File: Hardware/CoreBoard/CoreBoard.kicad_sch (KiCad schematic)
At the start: 86 parts, among them J1 RJ45_LED_Shielded, SW1 SW_Push, SW10 SW_Push, SW11 SW_Push, SW12 SW_Push, SW13 SW_Push, SW14 SW_Push, SW15 SW_Push, SW16 SW_SPDT, SW2 SW_Push, SW3 SW_Push, SW4 SW_Push, SW5 SW_Push, SW6 SW_Push, SW7 SW_Push, SW8 SW_Push, SW9 SW_Push, U1 Teensy4.1_DEV-16771, U3 SHHD003A0A, U4 74HC148, U5 74HC148, U6 74HC00, U7 OKI

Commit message: made rev2 changes and cleaned up traces
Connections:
- net +3V3: no longer U4.5 (EI)
- net BL_RX: now also Conn2.2, U1.34 (RX8); no longer Conn2.8, U1.35 (TX8)
- net BL_TX: now also Conn2.1, U1.35 (TX8); no longer Conn2.9, U1.30 (CRX3)
- net BR_RX: now also U1.15 (A1); no longer U1.17 (A3)
- net BR_TX: now also U1.14 (A0); no longer U1.16 (A2)
- net FL_RX: now also Conn2.8, U1.28 (RX7); no longer Conn2.2, U1.14 (A0)
- net FL_TX: now also Conn2.7, U1.29 (TX7); no longer Conn2.3, U1.38 (A14)
- net FR_RX: now also U1.21 (A7); no longer U1.23 (A9)
- net FR_TX: now also U1.20 (A6); no longer U1.22 (A8)
- net GND: now also Conn2.3, Conn2.6, Conn2.9, U4.5 (EI); no longer Conn2.1, Conn2.4, Conn2.7
- net ML_RX: now also U1.25 (A11); no longer U1.37 (CS3)
- net ML_TX: now also Conn2.4, U1.24 (A10); no longer Conn2.6, U1.36 (CS2)
- net MR_RX: now also U1.16 (A2); no longer U1.21 (A7)
- net MR_TX: now also U1.17 (A3); no longer U1.20 (A6)
- net Out2: now also U1.41 (A17); no longer U1.34 (RX8)
- net ServoPWM1: now also U1.0 (RX1); no longer U1.2 (OUT2)
- net ServoPWM2: now also U1.1 (TX1); no longer U1.3 (LRCLK2)
- net ServoPWM3: now also U1.2 (OUT2); no longer U1.4 (BCLK2)
- net ServoPWM4: now also U1.3 (LRCLK2); no longer U1.5 (IN2)
- net ServoPWM5: now also U1.4 (BCLK2); no longer U1.6 (OUT1D)
- net ServoPWM6: now also U1.5 (IN2); no longer U1.7 (RX2)
- net ServoPWM7: now also U1.6 (OUT1D); no longer U1.8 (TX2)
- net ServoPWM8: now also U1.7 (RX2); no longer U1.9 (OUT1C)
- net ServoPWM9: now also U1.8 (TX2); no longer U1.10 (CS1)
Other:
- note added: "exact changes from rev1: moved FR_TX to 20 moved FR_RX to 21 moved MR_TX to 17 moved MR_RX to 16 moved BR_TX to 14 moved BR_RX to 15 moved FL_TX to 29 moved FL_RX to 28 moved ML_TX to 24 moved ML_RX to 25 moved BL_TX to 35 moved BL_RX to 34 moved Out2 from 34 to 41 moved ServoPWM1 to 0 moved ServoPWM2 to 1 moved ServoPWM3 to 2 moved ServoPWM4 to 3 moved ServoPWM5 to 4 moved ServoPWM6 to 5 moved S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"
- moved on the sheet: U4, U5

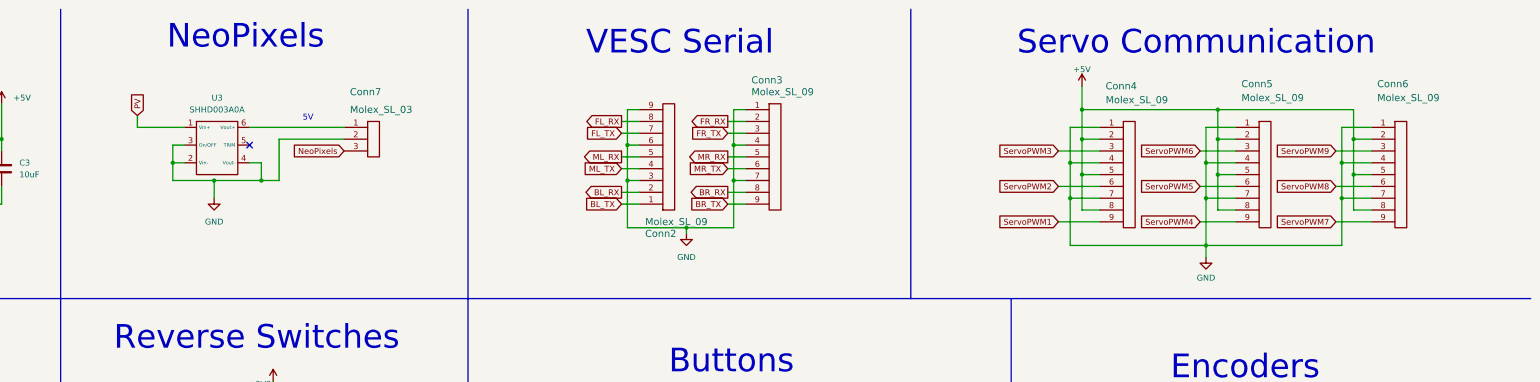
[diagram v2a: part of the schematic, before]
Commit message: added accelerometer and touch-ups
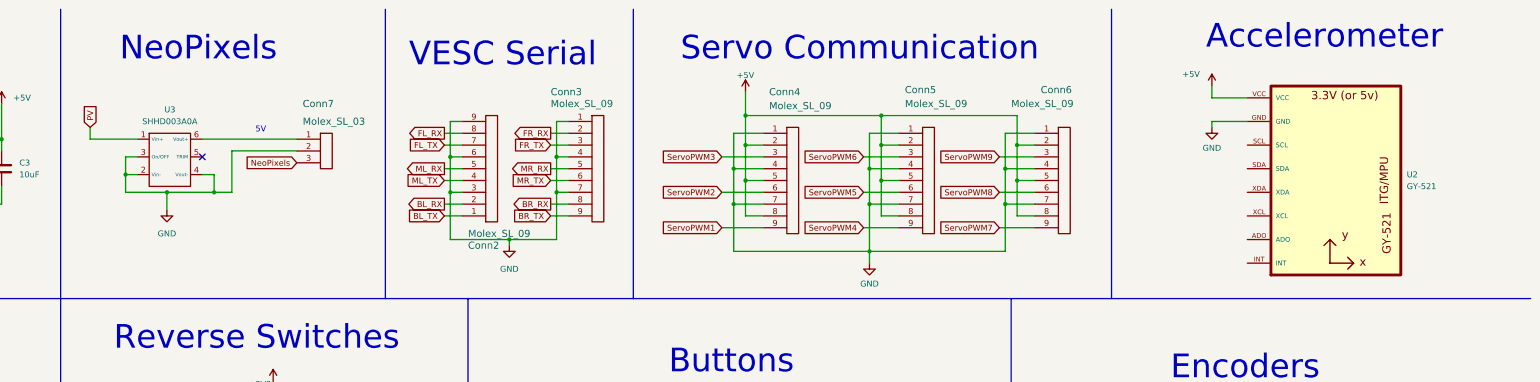
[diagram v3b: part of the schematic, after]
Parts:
- added U2: GY-521, GY-521:GY-521, symbol GY-521:GY-521
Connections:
- net +5V: now also U2.VCC
- net GND: now also U2.GND
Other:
- note added: "Accelerometer"
- moved on the sheet: Conn2, Conn3, Conn4, Conn5, Conn6, Conn7, U3

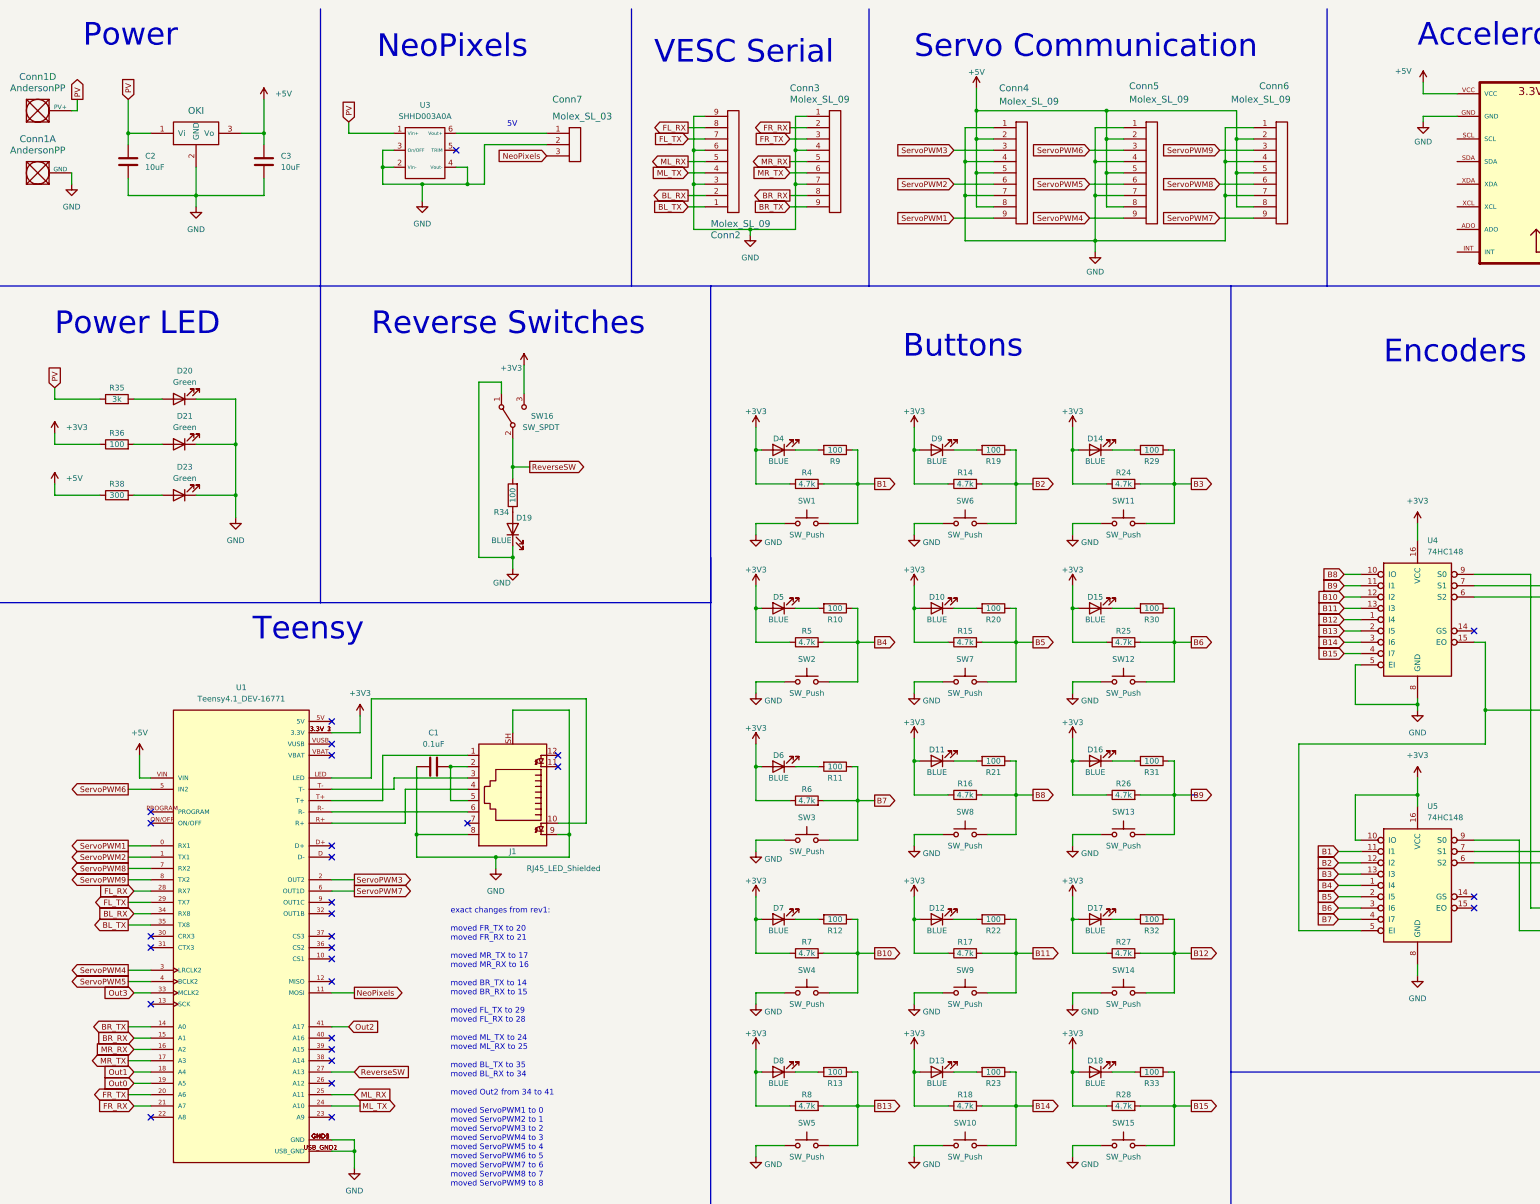
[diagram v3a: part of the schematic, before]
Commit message: finished adding accelerometer
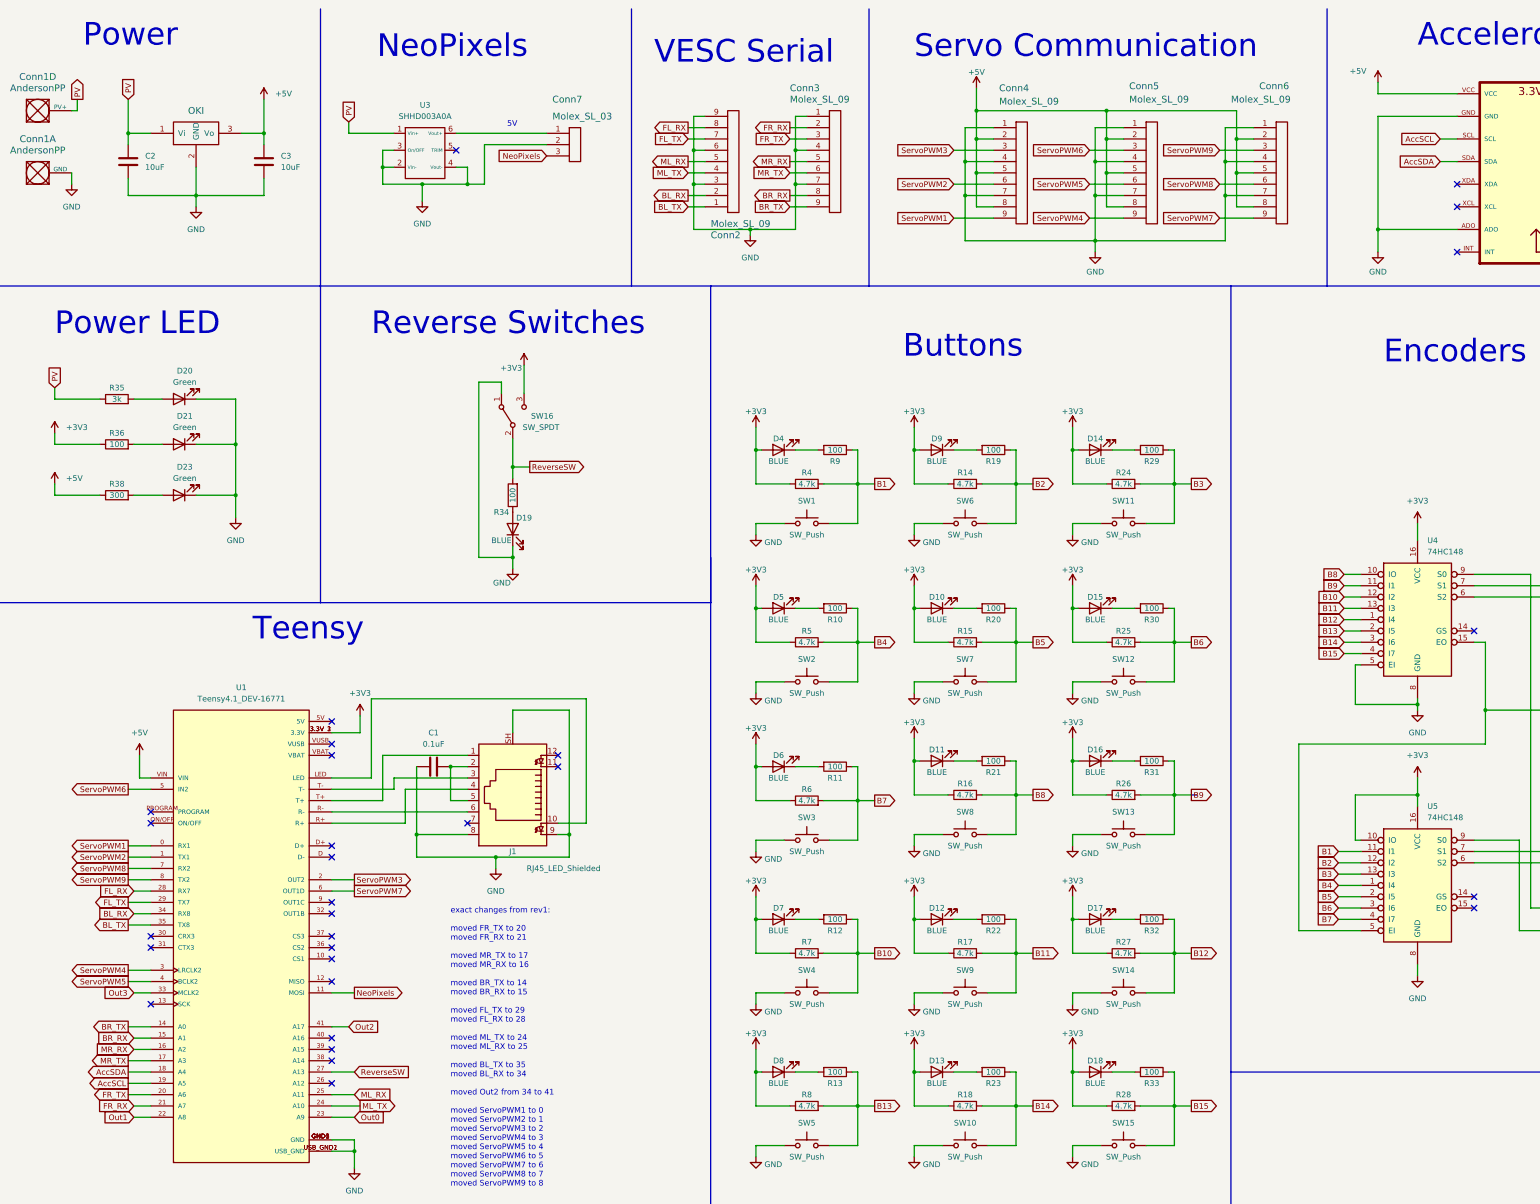
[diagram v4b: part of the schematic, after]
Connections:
- net GND: now also U2.ADO
- net Out0: now also U1.23 (A9); no longer U1.19 (A5)
- net Out1: now also U1.22 (A8); no longer U1.18 (A4)
- net AccSCL: now reaches U2.SCL
- net AccSCL: now also U1.19 (A5)
- net AccSDA: now reaches U2.SDA
- net AccSDA: now also U1.18 (A4)
- no-connect marks 29 -> 30
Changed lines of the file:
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@@
   (junction (at 224.79 251.46) (diameter 0) (color 0 0 0 0)
   )
+  (junction (at 328.93 62.23) (diameter 0) (color 0 0 0 0)
+  )
   (junction (at 63.5 54.61) (diameter 0) (color 0 0 0 0)
   )
@@
   (junction (at 337.82 168.91) (diameter 0) (color 0 0 0 0)
   )
+  (no_connect (at 346.71 67.31))
+  (no_connect (at 346.71 52.07))
   (no_connect (at 93.98 246.38))
   (no_connect (at 93.98 231.14))
-  (no_connect (at 53.34 261.62))
   (no_connect (at 93.98 177.8))
+  (no_connect (at 346.71 57.15))
   (no_connect (at 93.98 254))
   (no_connect (at 93.98 203.2))
@@
   (no_connect (at 350.52 212.09))
   (no_connect (at 124.46 195.58))
-  (no_connect (at 93.98 261.62))
   (no_connect (at 53.34 223.52))
   (no_connect (at 93.98 213.36))
@@
     (stroke (width 0) (type default))
   )
+  (wire (pts (xy 49.53 261.62) (xy 53.34 261.62))
+    (stroke (width 0) (type default))
+  )
   (wire (pts (xy 72.39 110.49) (xy 72.39 121.92))
     (stroke (width 0) (type default))
@@
     (stroke (width 0) (type default))
   )
-  (wire (pts (xy 49.53 254) (xy 53.34 254))
-    (stroke (width 0) (type default))
-  )
   (wire (pts (xy 134.62 109.22) (xy 134.62 115.57))
     (stroke (width 0) (type default))
@@
     (stroke (width 0) (type default))
   )
+  (wire (pts (xy 342.9 41.91) (xy 346.71 41.91))
+    (stroke (width 0) (type default))
+  )
   (wire (pts (xy 144.78 198.12) (xy 147.32 198.12))
     (stroke (width 0) (type default))
@@
     (stroke (width 0) (type default))
   )
-  (wire (pts (xy 339.09 31.75) (xy 339.09 29.21))
+  (wire (pts (xy 328.93 31.75) (xy 328.93 29.21))
     (stroke (width 0) (type default))
   )
@@
     (stroke (width 0) (type default))
   )
-  (wire (pts (xy 346.71 31.75) (xy 339.09 31.75))
+  (wire (pts (xy 346.71 31.75) (xy 328.93 31.75))
     (stroke (width 0) (type default))
   )
@@
     (stroke (width 0) (type default))
   )
+  (wire (pts (xy 93.98 261.62) (xy 99.06 261.62))
+    (stroke (width 0) (type default))
+  )
   (wire (pts (xy 246.38 251.46) (xy 247.65 251.46))
     (stroke (width 0) (type default))
@@
     (stroke (width 0) (type default))
   )
+  (wire (pts (xy 48.26 251.46) (xy 53.34 251.46))
+    (stroke (width 0) (type default))
+  )
   (wire (pts (xy 204.47 259.08) (xy 212.09 259.08))
     (stroke (width 0) (type default))
@@
     (stroke (width 0) (type default))
   )
+  (wire (pts (xy 328.93 62.23) (xy 328.93 67.31))
+    (stroke (width 0) (type default))
+  )
   (wire (pts (xy 353.06 154.94) (xy 350.52 154.94))
     (stroke (width 0) (type default))
@@
     (stroke (width 0) (type default))
   )
-  (wire (pts (xy 49.53 251.46) (xy 53.34 251.46))
-    (stroke (width 0) (type default))
-  )
   (wire (pts (xy 224.79 154.94) (xy 232.41 154.94))
     (stroke (width 0) (type default))
@@
     (stroke (width 0) (type default))
   )
-  (wire (pts (xy 339.09 36.83) (xy 339.09 38.1))
+  (wire (pts (xy 328.93 36.83) (xy 328.93 62.23))
     (stroke (width 0) (type default))
   )
-  (wire (pts (xy 346.71 36.83) (xy 339.09 36.83))
+  (wire (pts (xy 346.71 36.83) (xy 328.93 36.83))
     (stroke (width 0) (type default))
   )
@@
     (stroke (width 0) (type default))
   )
+  (wire (pts (xy 48.26 254) (xy 53.34 254))
+    (stroke (width 0) (type default))
+  )
   (wire (pts (xy 224.79 212.09) (xy 224.79 217.17))
     (stroke (width 0) (type default))
@@
     (stroke (width 0) (type default))
   )
+  (wire (pts (xy 342.9 46.99) (xy 346.71 46.99))
+    (stroke (width 0) (type default))
+  )
   (wire (pts (xy 276.86 233.68) (xy 283.21 233.68))
     (stroke (width 0) (type default))
@@
     (stroke (width 0) (type default))
   )
+  (wire (pts (xy 328.93 62.23) (xy 346.71 62.23))
+    (stroke (width 0) (type default))
+  )
   (wire (pts (xy 93.98 175.26) (xy 100.33 175.26))
     (stroke (width 0) (type default))
@@
     )
   )
-  (global_label "Out0" (shape input) (at 49.53 254 180) (fields_autoplaced)
-    (effects (font (size 1.27 1.27)) (justify right))
-    (property "Intersheetrefs" "${INTERSHEET_REFS}" (at 42.1301 254 0)
-      (effects (font (size 1.27 1.27)) (justify right) hide)
+  (global_label "Out0" (shape input) (at 99.06 261.62 0) (fields_autoplaced)
+    (effects (font (size 1.27 1.27)) (justify left))
+    (property "Intersheetrefs" "${INTERSHEET_REFS}" (at 106.4599 261.62 0)
+      (effects (font (size 1.27 1.27)) (justify left) hide)
     )
   )
@@
     )
   )
+  (global_label "AccSDA" (shape input) (at 342.9 46.99 180) (fields_autoplaced)
+    (effects (font (size 1.27 1.27)) (justify right))
+    (property "Intersheetrefs" "${INTERSHEET_REFS}" (at 333.0809 46.99 0)
+      (effects (font (size 1.27 1.27)) (justify right) hide)
+    )
+  )
   (global_label "FL_RX" (shape input) (at 49.53 210.82 180) (fields_autoplaced)
     (effects (font (size 1.27 1.27)) (justify right))
@@
     )
   )
+  (global_label "AccSCL" (shape output) (at 48.26 254 180) (fields_autoplaced)
+    (effects (font (size 1.27 1.27)) (justify right))
+    (property "Intersheetrefs" "${INTERSHEET_REFS}" (at 38.5014 254 0)
+      (effects (font (size 1.27 1.27)) (justify right) hide)
+    )
+  )
   (global_label "MR_TX" (shape output) (at 48.26 248.92 180) (fields_autoplaced)
     (effects (font (size 1.27 1.27)) (justify right))
@@
     )
   )
+  (global_label "AccSCL" (shape input) (at 342.9 41.91 180) (fields_autoplaced)
+    (effects (font (size 1.27 1.27)) (justify right))
+    (property "Intersheetrefs" "${INTERSHEET_REFS}" (at 333.1414 41.91 0)
+      (effects (font (size 1.27 1.27)) (justify right) hide)
+    )
+  )
   (global_label "ServoPWM7" (shape output) (at 99.06 210.82 0) (fields_autoplaced)
     (effects (font (size 1.27 1.27)) (justify left))
@@
     )
   )
+  (global_label "AccSDA" (shape output) (at 48.26 251.46 180) (fields_autoplaced)
+    (effects (font (size 1.27 1.27)) (justify right))
+    (property "Intersheetrefs" "${INTERSHEET_REFS}" (at 38.4409 251.46 0)
+      (effects (font (size 1.27 1.27)) (justify right) hide)
+    )
+  )
   (global_label "FR_RX" (shape output) (at 196.85 39.37 180) (fields_autoplaced)
     (effects (font (size 1.27 1.27)) (justify right))
@@
     )
   )
-  (global_label "Out1" (shape input) (at 49.53 251.46 180) (fields_autoplaced)
+  (global_label "Out1" (shape input) (at 49.53 261.62 180) (fields_autoplaced)
     (effects (font (size 1.27 1.27)) (justify right))
-    (property "Intersheetrefs" "${INTERSHEET_REFS}" (at 42.1301 251.46 0)
+    (property "Intersheetrefs" "${INTERSHEET_REFS}" (at 42.1301 261.62 0)
       (effects (font (size 1.27 1.27)) (justify right) hide)
     )
@@
     )
   )
-  (symbol (lib_id "power:GND") (at 339.09 38.1 0) (unit 1)
+  (symbol (lib_id "power:GND") (at 328.93 67.31 0) (unit 1)
     (in_bom yes) (on_board yes) (dnp no) (fields_autoplaced)
-    (property "Reference" "#PWR053" (at 339.09 44.45 0)
+    (property "Reference" "#PWR053" (at 328.93 73.66 0)
       (effects (font (size 1.27 1.27)) hide)
     )
-    (property "Value" "GND" (at 339.09 42.5434 0)
+    (property "Value" "GND" (at 328.93 71.7534 0)
       (effects (font (size 1.27 1.27)))
     )
-    (property "Footprint" "" (at 339.09 38.1 0)
+    (property "Footprint" "" (at 328.93 67.31 0)
       (effects (font (size 1.27 1.27)) hide)
     )
-    (property "Datasheet" "" (at 339.09 38.1 0)
+    (property "Datasheet" "" (at 328.93 67.31 0)
       (effects (font (size 1.27 1.27)) hide)
     )
@@
     )
   )
-  (symbol (lib_id "power:+5V") (at 339.09 29.21 0) (unit 1)
+  (symbol (lib_id "power:+5V") (at 328.93 29.21 0) (unit 1)
     (in_bom yes) (on_board yes) (dnp no)
-    (property "Reference" "#PWR052" (at 339.09 33.02 0)
+    (property "Reference" "#PWR052" (at 328.93 33.02 0)
       (effects (font (size 1.27 1.27)) hide)
     )
-    (property "Value" "+5V" (at 332.74 26.67 0)
+    (property "Value" "+5V" (at 322.58 26.67 0)
       (effects (font (size 1.27 1.27)) (justify left))
     )
-    (property "Footprint" "" (at 339.09 29.21 0)
+    (property "Footprint" "" (at 328.93 29.21 0)
       (effects (font (size 1.27 1.27)) hide)
     )
-    (property "Datasheet" "" (at 339.09 29.21 0)
+    (property "Datasheet" "" (at 328.93 29.21 0)
       (effects (font (size 1.27 1.27)) hide)
     )
